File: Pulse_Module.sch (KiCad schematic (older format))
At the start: 5 parts, among them CON3 BARREL_JACK, U3 AMS1117

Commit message: Последние изменения
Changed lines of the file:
@@
-$EndComp
-$Comp
-L GND #PWR04
-U 1 1 57F30351
-P 4155 6805
-F 0 "#PWR04" H 4155 6555 50  0001 C CNN
-F 1 "GND" H 4155 6655 50  0000 C CNN
-F 2 "" H 4155 6805 50  0000 C CNN
-F 3 "" H 4155 6805 50  0000 C CNN
-	1    4155 6805
-	1    0    0    -1
 $EndComp
 $Comp

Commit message: Последние изменения на плате
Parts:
- added R9: R, Resistors_SMD:R_0805, symbol R
- added RV2: POT, Potentiometers:Potentiometer_Bourns_3296W_3-8Zoll_Inline_ScrewUp, symbol POT
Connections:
- net GND: now also RV2.1; no longer U3.1 (GND/ADJ)
- net Sheet56DEE0DD/VCC_3.3: now also R9.1
- new net: R9.2, RV2.2, RV2.3, U3.1 (GND/ADJ)
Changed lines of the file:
@@
 L GND #PWR02
 U 1 1 57F2F7B1
-P 4180 5785
-F 0 "#PWR02" H 4180 5535 50  0001 C CNN
-F 1 "GND" H 4180 5635 50  0000 C CNN
-F 2 "" H 4180 5785 50  0000 C CNN
-F 3 "" H 4180 5785 50  0000 C CNN
-	1    4180 5785
+P 4180 6090
+F 0 "#PWR02" H 4180 5840 50  0001 C CNN
+F 1 "GND" H 4180 5940 50  0000 C CNN
+F 2 "" H 4180 6090 50  0000 C CNN
+F 3 "" H 4180 6090 50  0000 C CNN
+	1    4180 6090
 	1    0    0    -1
 $EndComp
@@
 	1    0    0    -1
 $EndComp
+$Comp
+L R R9
+U 1 1 57FA70B5
+P 4835 5300
+F 0 "R9" V 4915 5300 50  0000 C CNN
+F 1 "R" V 4835 5300 50  0000 C CNN
+F 2 "Resistors_SMD:R_0805" V 4765 5300 50  0001 C CNN
+F 3 "" H 4835 5300 50  0000 C CNN
+	1    4835 5300
+	1    0    0    -1
+$EndComp
+$Comp
+L POT RV2
+U 1 1 57FA714E
+P 4835 5750
+F 0 "RV2" H 4835 5670 50  0000 C CNN
+F 1 "POT" H 4835 5750 50  0000 C CNN
+F 2 "Potentiometers:Potentiometer_Bourns_3296W_3-8Zoll_Inline_ScrewUp" H 4835 5750 50  0001 C CNN
+F 3 "" H 4835 5750 50  0000 C CNN
+	1    4835 5750
+	0    -1   -1   0
+$EndComp
 Wire Wire Line
 	2350 3750 3000 3750
@@
 	4395 4650 5045 4650
 Wire Wire Line
-	5045 4650 5045 4945
+	5045 4650 5045 5000
 Connection ~ 5045 4945
 Wire Wire Line
-	3085 5370 3085 5615
+	3085 5370 3085 6010
 Wire Wire Line
-	3085 5615 5210 5615
+	5210 5365 5210 6010
 Wire Wire Line
-	5210 5615 5210 5365
+	4835 5150 4835 5000
 Wire Wire Line
-	4180 5445 4180 5785
-Connection ~ 4180 5615
+	4835 5000 5045 5000
+Wire Wire Line
+	4180 5550 4835 5550
+Wire Wire Line
+	4835 5450 4835 5600
+Connection ~ 4180 5550
+Connection ~ 4835 5550
+Wire Wire Line
+	4505 5550 4505 5750
+Wire Wire Line
+	4505 5750 4685 5750
+Connection ~ 4505 5550
+Wire Wire Line
+	4180 5445 4180 5550
+Wire Wire Line
+	5210 6010 3085 6010
+Wire Wire Line
+	4835 5900 4835 6010
+Connection ~ 4835 6010
+Wire Wire Line
+	4180 6090 4180 6010
+Connection ~ 4180 6010
 $EndSCHEMATC

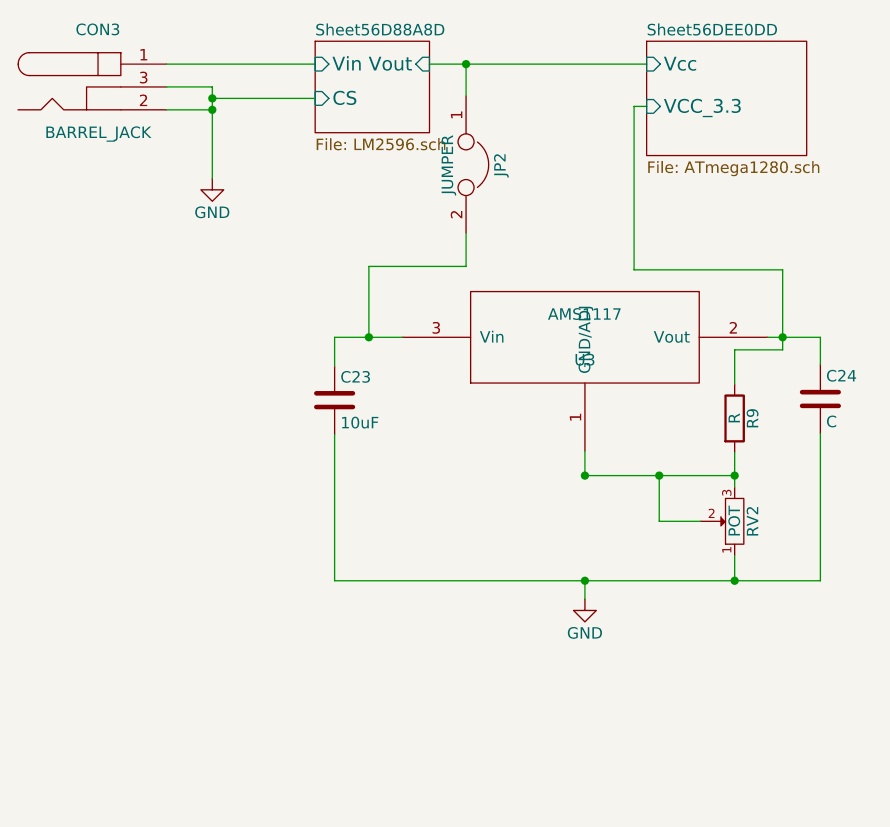
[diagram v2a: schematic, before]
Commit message: перенесён футпринт С1 вперёд
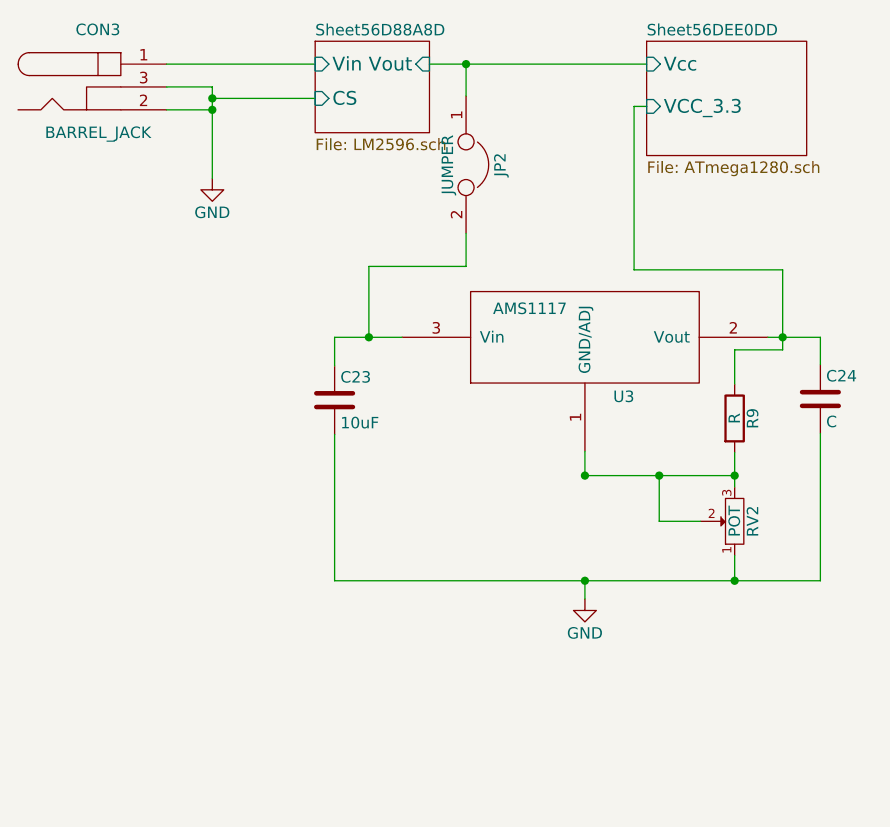
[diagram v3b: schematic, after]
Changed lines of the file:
@@
 U 1 1 57F689F7
 P 4180 4945
-F 0 "U3" H 4180 4845 50  0000 C CNN
-F 1 "AMS1117" H 4180 5045 50  0000 C CNN
+F 0 "U3" H 4350 4685 50  0000 C CNN
+F 1 "AMS1117" H 3940 5070 50  0000 C CNN
 F 2 "TO_SOT_Packages_SMD:TO-252-2Lead" H 4180 4945 60  0001 C CNN
 F 3 "" H 4180 4945 60  0000 C CNN

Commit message: Точно последняя версия
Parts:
- U3: footprint TO_SOT_Packages_SMD:TO-252-2Lead -> TO_SOT_Packages_SMD:SOT-223
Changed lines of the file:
@@
 LIBS:display
 LIBS:ws2812
+LIBS:open-project
 LIBS:cypress
 LIBS:siliconi
@@
 F 0 "U3" H 4350 4685 50  0000 C CNN
 F 1 "AMS1117" H 3940 5070 50  0000 C CNN
-F 2 "TO_SOT_Packages_SMD:TO-252-2Lead" H 4180 4945 60  0001 C CNN
+F 2 "TO_SOT_Packages_SMD:SOT-223" H 4180 4945 60  0001 C CNN
 F 3 "" H 4180 4945 60  0000 C CNN
 	1    4180 4945
